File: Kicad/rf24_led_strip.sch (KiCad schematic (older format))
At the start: 27 parts, among them IC1 ATMEGA328-P, P1 UART, P2 12V in, P3 LED_OUT, Q1 Q_NMOS_GDS, Q2 Q_NMOS_GDS, Q3 Q_NMOS_GDS, U1 LM_1117, U2 LM_1117, U3 nrf24l01+

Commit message: 3.3V Version.
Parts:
- removed C2: C, Capacitors_SMD:C_0603_HandSoldering, symbol C
- removed R10, R11: R, Resistors_SMD:R_0805, symbol R
- removed U1: LM_1117, TO_SOT_Packages_SMD:SOT-223, symbol LM_1117
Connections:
- net labels removed: +5V
- wire segments 79 -> 71
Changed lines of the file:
@@
 	3550 4550 3300 4550
 Connection ~ 3550 4550
-$Comp
-L +5V #PWR05
-U 1 1 56C79115
-P 3300 2300
-F 0 "#PWR05" H 3300 2150 50  0001 C CNN
-F 1 "+5V" H 3300 2440 50  0000 C CNN
-F 2 "" H 3300 2300 60  0000 C CNN
-F 3 "" H 3300 2300 60  0000 C CNN
-	1    3300 2300
-	0    -1   -1   0
-$EndComp
 Wire Wire Line
 	3300 2300 3550 2300
@@
 Connection ~ 3350 2300
 $Comp
-L GND #PWR06
+L GND #PWR05
 U 1 1 56C7929B
 P 3350 2750
-F 0 "#PWR06" H 3350 2500 50  0001 C CNN
+F 0 "#PWR05" H 3350 2500 50  0001 C CNN
 F 1 "GND" H 3350 2600 50  0000 C CNN
 F 2 "" H 3350 2750 60  0000 C CNN
@@
 $EndComp
 $Comp
-L +12V #PWR07
+L +12V #PWR06
 U 1 1 56C796A5
-P 4600 1100
-F 0 "#PWR07" H 4600 950 50  0001 C CNN
-F 1 "+12V" H 4600 1240 50  0000 C CNN
-F 2 "" H 4600 1100 60  0000 C CNN
-F 3 "" H 4600 1100 60  0000 C CNN
-	1    4600 1100
-	0    -1   -1   0
-$EndComp
-$Comp
-L GND #PWR08
-U 1 1 56C796DA
 P 4700 1200
-F 0 "#PWR08" H 4700 950 50  0001 C CNN
-F 1 "GND" H 4700 1050 50  0000 C CNN
+F 0 "#PWR06" H 4700 1050 50  0001 C CNN
+F 1 "+12V" H 4700 1340 50  0000 C CNN
 F 2 "" H 4700 1200 60  0000 C CNN
 F 3 "" H 4700 1200 60  0000 C CNN
 	1    4700 1200
+	0    -1   -1   0
+$EndComp
+$Comp
+L GND #PWR07
+U 1 1 56C796DA
+P 4500 1100
+F 0 "#PWR07" H 4500 850 50  0001 C CNN
+F 1 "GND" H 4500 950 50  0000 C CNN
+F 2 "" H 4500 1100 60  0000 C CNN
+F 3 "" H 4500 1100 60  0000 C CNN
+	1    4500 1100
 	0    1    1    0
 $EndComp
@@
 	4700 1200 4850 1200
 Wire Wire Line
-	4600 1100 4850 1100
+	4500 1100 4850 1100
 $Comp
 L CONN_01X04 P3
@@
 $EndComp
 $Comp
-L +12V #PWR09
+L +12V #PWR08
 U 1 1 56C7A172
 P 5850 1100
-F 0 "#PWR09" H 5850 950 50  0001 C CNN
+F 0 "#PWR08" H 5850 950 50  0001 C CNN
 F 1 "+12V" H 5850 1240 50  0000 C CNN
 F 2 "" H 5850 1100 60  0000 C CNN
@@
 $EndComp
 $Comp
-L GND #PWR010
+L GND #PWR09
 U 1 1 56C7A8FA
 P 8150 4650
-F 0 "#PWR010" H 8150 4400 50  0001 C CNN
+F 0 "#PWR09" H 8150 4400 50  0001 C CNN
 F 1 "GND" H 8150 4500 50  0000 C CNN
 F 2 "" H 8150 4650 60  0000 C CNN
@@
 $EndComp
 $Comp
-L GND #PWR011
+L GND #PWR010
 U 1 1 56C7BD3D
 P 10250 4800
-F 0 "#PWR011" H 10250 4550 50  0001 C CNN
+F 0 "#PWR010" H 10250 4550 50  0001 C CNN
 F 1 "GND" H 10250 4650 50  0000 C CNN
 F 2 "" H 10250 4800 60  0000 C CNN
@@
 $EndComp
 $Comp
-L GND #PWR012
+L GND #PWR011
 U 1 1 56C7BF2D
 P 8150 5950
-F 0 "#PWR012" H 8150 5700 50  0001 C CNN
+F 0 "#PWR011" H 8150 5700 50  0001 C CNN
 F 1 "GND" H 8150 5800 50  0000 C CNN
 F 2 "" H 8150 5950 60  0000 C CNN
@@
 Wire Wire Line
 	6750 5450 7250 5450
-Text Label 6000 2300 2    60   ~ 0
+Text Label 6000 2500 2    60   ~ 0
 RED_PWM
 Wire Wire Line
@@
 Wire Wire Line
 	6000 2500 5450 2500
-Text Label 6000 2500 2    60   ~ 0
+Text Label 6000 2300 2    60   ~ 0
 BLUE_PWM
-Wire Wire Line
-	6000 2300 5450 2300
-$Comp
-L +5V #PWR013
-U 1 1 56C7D2C5
-P 6600 3750
-F 0 "#PWR013" H 6600 3600 50  0001 C CNN
-F 1 "+5V" H 6600 3890 50  0000 C CNN
-F 2 "" H 6600 3750 60  0000 C CNN
-F 3 "" H 6600 3750 60  0000 C CNN
-	1    6600 3750
-	0    1    1    0
-$EndComp
 $Comp
 L R R1
@@
 $EndComp
 $Comp
-L GND #PWR014
+L GND #PWR012
 U 1 1 56C7DDEB
 P 1900 3000
-F 0 "#PWR014" H 1900 2750 50  0001 C CNN
+F 0 "#PWR012" H 1900 2750 50  0001 C CNN
 F 1 "GND" H 1900 2850 50  0000 C CNN
 F 2 "" H 1900 3000 60  0000 C CNN
@@
 Wire Wire Line
 	2200 3000 2200 3300
+Text Label 2100 3000 3    60   ~ 0
+TX
 Text Label 2000 3000 3    60   ~ 0
-TX
-Text Label 2100 3000 3    60   ~ 0
 RX
 Wire Wire Line
@@
 	6100 4300 6100 4100
 $Comp
-L +12V #PWR015
+L +12V #PWR013
 U 1 1 56C7FD64
 P 1450 6300
-F 0 "#PWR015" H 1450 6150 50  0001 C CNN
+F 0 "#PWR013" H 1450 6150 50  0001 C CNN
 F 1 "+12V" H 1450 6440 50  0000 C CNN
 F 2 "" H 1450 6300 60  0000 C CNN
@@
 $EndComp
 $Comp
-L GND #PWR016
+L GND #PWR014
 U 1 1 56C7FDAE
 P 1750 6300
-F 0 "#PWR016" H 1750 6050 50  0001 C CNN
+F 0 "#PWR014" H 1750 6050 50  0001 C CNN
 F 1 "GND" H 1750 6150 50  0000 C CNN
 F 2 "" H 1750 6300 60  0000 C CNN
@@
 $EndComp
 $Comp
-L PWR_FLAG #FLG017
+L PWR_FLAG #FLG015
 U 1 1 56C7FEB7
 P 1450 6700
-F 0 "#FLG017" H 1450 6795 50  0001 C CNN
+F 0 "#FLG015" H 1450 6795 50  0001 C CNN
 F 1 "PWR_FLAG" H 1450 6880 50  0000 C CNN
 F 2 "" H 1450 6700 60  0000 C CNN
@@
 $EndComp
 $Comp
-L PWR_FLAG #FLG018
+L PWR_FLAG #FLG016
 U 1 1 56C7FF13
 P 1750 6700
-F 0 "#FLG018" H 1750 6795 50  0001 C CNN
+F 0 "#FLG016" H 1750 6795 50  0001 C CNN
 F 1 "PWR_FLAG" H 1750 6880 50  0000 C CNN
 F 2 "" H 1750 6700 60  0000 C CNN
@@
 NoConn ~ 3550 2900
 $Comp
-L +3.3V #PWR019
+L +3.3V #PWR017
 U 1 1 56C83337
 P 4650 5950
-F 0 "#PWR019" H 4650 5800 50  0001 C CNN
+F 0 "#PWR017" H 4650 5800 50  0001 C CNN
 F 1 "+3.3V" H 4650 6090 50  0000 C CNN
 F 2 "" H 4650 5950 60  0000 C CNN
@@
 MISO
 $Comp
-L GND #PWR020
+L GND #PWR018
 U 1 1 56C83AE6
 P 3300 5950
-F 0 "#PWR020" H 3300 5700 50  0001 C CNN
+F 0 "#PWR018" H 3300 5700 50  0001 C CNN
 F 1 "GND" H 3300 5800 50  0000 C CNN
 F 2 "" H 3300 5950 60  0000 C CNN
@@
 Wire Wire Line
 	8850 1200 8900 1200
-$Comp
-L R R10
-U 1 1 56D08DC0
-P 2000 1850
-F 0 "R10" V 2080 1850 50  0000 C CNN
-F 1 "R" V 2000 1850 50  0000 C CNN
-F 2 "Resistors_SMD:R_0805" V 1930 1850 30  0001 C CNN
-F 3 "" H 2000 1850 30  0000 C CNN
-	1    2000 1850
-	1    0    0    -1
-$EndComp
-$Comp
-L R R11
-U 1 1 56D08DC6
-P 2350 1700
-F 0 "R11" V 2430 1700 50  0000 C CNN
-F 1 "R" V 2350 1700 50  0000 C CNN
-F 2 "Resistors_SMD:R_0805" V 2280 1700 30  0001 C CNN
-F 3 "" H 2350 1700 30  0000 C CNN
-	1    2350 1700
-	0    -1   -1   0
-$EndComp
-Wire Wire Line
-	2000 1700 2000 1400
-$Comp
-L C C1
-U 1 1 56D08DCD
-P 1400 1400
-F 0 "C1" H 1425 1500 50  0000 L CNN
-F 1 "C" H 1425 1300 50  0000 L CNN
-F 2 "Capacitors_SMD:C_0603_HandSoldering" H 1438 1250 30  0001 C CNN
-F 3 "" H 1400 1400 60  0000 C CNN
-	1    1400 1400
-	-1   0    0    1
-$EndComp
-$Comp
-L C C2
-U 1 1 56D08DD3
-P 2500 1950
-F 0 "C2" H 2525 2050 50  0000 L CNN
-F 1 "C" H 2525 1850 50  0000 L CNN
-F 2 "Capacitors_SMD:C_0603_HandSoldering" H 2538 1800 30  0001 C CNN
-F 3 "" H 2500 1950 60  0000 C CNN
-	1    2500 1950
-	-1   0    0    1
-$EndComp
-Wire Wire Line
-	2500 900  2500 1800
-Wire Wire Line
-	1400 1550 1400 2100
-Connection ~ 2000 1700
-$Comp
-L +12V #PWR021
-U 1 1 56D08DDC
-P 1100 1000
-F 0 "#PWR021" H 1100 850 50  0001 C CNN
-F 1 "+12V" H 1100 1140 50  0000 C CNN
-F 2 "" H 1100 1000 60  0000 C CNN
-F 3 "" H 1100 1000 60  0000 C CNN
-	1    1100 1000
-	0    -1   -1   0
-$EndComp
-Wire Wire Line
-	2000 1700 2200 1700
-Wire Wire Line
-	1400 2100 2500 2100
-Wire Wire Line
-	2000 2000 2000 2250
-$Comp
-L GND #PWR022
-U 1 1 56D08DE5
-P 2000 2250
-F 0 "#PWR022" H 2000 2000 50  0001 C CNN
-F 1 "GND" H 2000 2100 50  0000 C CNN
-F 2 "" H 2000 2250 60  0000 C CNN
-F 3 "" H 2000 2250 60  0000 C CNN
-	1    2000 2250
-	1    0    0    -1
-$EndComp
-Connection ~ 2000 2100
-Connection ~ 2500 1700
-$Comp
-L LM_1117 U1
-U 1 1 56D08DF3
-P 1950 700
-F 0 "U1" H 2150 150 60  0000 C CNN
-F 1 "LM_1117" H 1950 700 60  0000 C CNN
-F 2 "TO_SOT_Packages_SMD:SOT-223" H 1950 700 60  0001 C CNN
-F 3 "" H 1950 700 60  0000 C CNN
-	1    1950 700
-	1    0    0    -1
-$EndComp
-Wire Wire Line
-	1100 1000 1550 1000
-Wire Wire Line
-	1400 1250 1400 1000
-Connection ~ 1400 1000
-Wire Wire Line
-	2450 1000 2800 1000
-Connection ~ 2500 1000
-Wire Wire Line
-	2450 900  2500 900
-$Comp
-L +5V #PWR023
-U 1 1 56D097BC
-P 2800 1000
-F 0 "#PWR023" H 2800 850 50  0001 C CNN
-F 1 "+5V" H 2800 1140 50  0000 C CNN
-F 2 "" H 2800 1000 60  0000 C CNN
-F 3 "" H 2800 1000 60  0000 C CNN
-	1    2800 1000
-	0    1    1    0
-$EndComp
 NoConn ~ 3550 3650
 NoConn ~ 3550 3750
@@
 NoConn ~ 5450 2900
 NoConn ~ 5450 3000
+$Comp
+L +3.3V #PWR019
+U 1 1 589CA4C6
+P 3300 2300
+F 0 "#PWR019" H 3300 2150 50  0001 C CNN
+F 1 "+3.3V" H 3300 2440 50  0000 C CNN
+F 2 "" H 3300 2300 60  0000 C CNN
+F 3 "" H 3300 2300 60  0000 C CNN
+	1    3300 2300
+	0    -1   -1   0
+$EndComp
+$Comp
+L +3.3V #PWR020
+U 1 1 589CAA46
+P 6600 3750
+F 0 "#PWR020" H 6600 3600 50  0001 C CNN
+F 1 "+3.3V" H 6600 3890 50  0000 C CNN
+F 2 "" H 6600 3750 60  0000 C CNN
+F 3 "" H 6600 3750 60  0000 C CNN
+	1    6600 3750
+	0    1    1    0
+$EndComp
+Wire Wire Line
+	5450 2300 6000 2300
+$Comp
+L C C1
+U 1 1 589CC8B0
+P 4500 5750
+F 0 "C1" H 4525 5850 50  0000 L CNN
+F 1 "C" H 4525 5650 50  0000 L CNN
+F 2 "Capacitors_SMD:C_0603_HandSoldering" H 4538 5600 30  0001 C CNN
+F 3 "" H 4500 5750 60  0000 C CNN
+	1    4500 5750
+	-1   0    0    1
+$EndComp
+$Comp
+L GND #PWR021
+U 1 1 589CCE09
+P 4500 5550
+F 0 "#PWR021" H 4500 5300 50  0001 C CNN
+F 1 "GND" H 4500 5400 50  0000 C CNN
+F 2 "" H 4500 5550 60  0000 C CNN
+F 3 "" H 4500 5550 60  0000 C CNN
+	1    4500 5550
+	-1   0    0    1
+$EndComp
+Wire Wire Line
+	4500 5600 4500 5550
+Wire Wire Line
+	4500 5900 4500 5950
+Connection ~ 4500 5950
 $EndSCHEMATC

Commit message: Update
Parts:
- added C10: 10µF, Capacitors_SMD:C_0805, symbol C
- added C11: 100µF, Capacitors_ThroughHole:CP_Radial_D6.3mm_P2.50mm, symbol CP
- added C2, C5: C, Capacitors_ThroughHole:C_Disc_D3.0mm_W2.0mm_P2.50mm, symbol C
- added C6, C9: C, Capacitors_SMD:C_0603_HandSoldering, symbol C
- added JP1: 5V, Connect:GS2, symbol Jumper_NO_Small
- added JP2: 12V, Connect:GS2, symbol Jumper_NO_Small
- added P4: LED3_OUT, Pin_Headers:Pin_Header_Straight_1x04_Pitch2.54mm, symbol CONN_01X04
- added P5: LED2_OUT, Pin_Headers:Pin_Header_Straight_1x04_Pitch2.54mm, symbol CONN_01X04
- added P6: WS2812, Pin_Headers:Pin_Header_Straight_1x03_Pitch2.54mm, symbol CONN_01X03
- added Q4, Q5, Q6, Q7, Q8, Q9: Q_NMOS_GDS, TO_SOT_Packages_SMD:SOT-23, symbol Q_NMOS_GSD
- added R10, R11, R12, R13, R14, R15, R16, R17, R18, R19, R20, R21, R22, R23, R24, R25, R26, R27: R, Resistors_SMD:R_0805, symbol R
- added U1: LM_1117, TO_SOT_Packages_SMD:SOT-223, symbol LM_1117
- added U4: ESP-01, Pin_Headers:Pin_Header_Straight_2x04_Pitch2.54mm, symbol ESP-01
- added Y1: Crystal, Crystals:Crystal_HC49-4H_Vertical, symbol Crystal
- C1: value C -> 100nF
- P1, P3: footprint Pin_Headers:Pin_Header_Straight_1x04 -> Pin_Headers:Pin_Header_Straight_1x04_Pitch2.54mm
- U3: footprint Socket_Strips:Socket_Strip_Straight_2x04 -> Pin_Headers:Pin_Header_Straight_2x04_Pitch2.54mm
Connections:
- net labels added: +5V, BLUE2, BLUE2_PWM, BLUE3, BLUE3_PWM, GREEN2, GREEN2_PWM, GREEN3, GREEN3_PWM, RED2, RED2_PWM, RED3, RED3_PWM, VCC
- wire segments 71 -> 164
- no-connect marks 14 -> 5
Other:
- moved on the sheet: C1, C3, C4, C7, C8, P1, P2, P3, Q1, Q2, Q3, R1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

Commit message: STM32 schematic done.
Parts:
- removed C11: 100µF, Capacitors_ThroughHole:CP_Radial_D6.3mm_P2.50mm, symbol CP
- removed C3, C4: C, Capacitors_SMD:C_0603_HandSoldering, symbol C
- removed IC1: ATMEGA328-P, Housings_QFP:TQFP-32_7x7mm_Pitch0.8mm, symbol ATMEGA328P-A
- removed JP1: 5V, Connect:GS2, symbol Jumper_NO_Small
- removed JP2: 12V, Connect:GS2, symbol Jumper_NO_Small
- removed P6: WS2812, Pin_Headers:Pin_Header_Straight_1x03_Pitch2.54mm, symbol CONN_01X03
- removed R1, R22: R, Resistors_SMD:R_0805, symbol R
- removed U1: LM_1117, TO_SOT_Packages_SMD:SOT-223, symbol LM_1117
- added C10: 10µF, Capacitors_SMD:C_0805, symbol C
- added C11, C12, C13, C14: 100nF, Capacitors_SMD:C_0603_HandSoldering, symbol C
- added D1: D, Diodes_ThroughHole:D_DO-15_P12.70mm_Horizontal, symbol D
- added JP1, JP2: Jumper, Pin_Headers:Pin_Header_Straight_1x02_Pitch2.54mm, symbol Jumper
- added P11: CONN_01X07, Pin_Headers:Pin_Header_Straight_1x07_Pitch2.54mm, symbol CONN_01X07
- added P5: LED4_OUT, Pin_Headers:Pin_Header_Straight_1x04_Pitch2.54mm, symbol CONN_01X04
- added P6: LED5_OUT, Pin_Headers:Pin_Header_Straight_1x04_Pitch2.54mm, symbol CONN_01X04
- added P7: USB_OTG, Connect:USB_Micro-B, symbol USB_OTG
- added P8: CONN_01X04, Pin_Headers:Pin_Header_Straight_1x04_Pitch2.54mm, symbol CONN_01X04
- added Q11, Q12, Q13, Q14, Q15, Q16: Q_NMOS_GDS, TO_SOT_Packages_SMD:SOT-23, symbol Q_NMOS_GSD
- added R26, R27, R28, R29, R30, R31, R32, R33, R34, R35, R36, R37, R40, R41: R, Resistors_SMD:R_0805, symbol R
- added U3: STM32F103C8Tx, Housings_QFP:LQFP-48_7x7mm_Pitch0.5mm, symbol STM32F103C8Tx
- C6, C9: value C -> 100nF
- renumbered C10 to C2, C5 to C4, C2 to C5, P2 to P1, P3 to P2, P5 to P3, P1 to P9, Q9 to Q10, Q1 to Q2, Q2 to Q4, Q4 to Q6, Q6 to Q7, Q7 to Q9, R12 to R11, R14 to R12, R15 to R14, R26 to R15, R27 to R16, R16 to R18, R18 to R19, R19 to R21, R21 to R22, R2 to R3, R6 to R38, R7 to R39, R8 to R4, R3 to R5, R4 to R6, R9 to R7, R5 to R8, R11 to R9, U3 to U1, U4 to U2, U2 to U4
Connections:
- net labels added: BLUE4, BLUE4_PWM, BLUE5, BLUE5_PWM, BOOT0, BOOT1, EXTRA1, EXTRA2, EXTRA3, EXTRA4, EXTRA5, EXTRA6, EXTRA7, GREEN4, GREEN4_PWM, GREEN5, GREEN5_PWM, NRST, RED4, RED4_PWM, RED5, RED5_PWM, SWD_CLK, SWD_IO, USB_DM, USB_DP
- net labels removed: +5V, DTR
- wire segments 164 -> 250
- no-connect marks 5 -> 4
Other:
- moved on the sheet: C1, C2, C4, C5, C7, C8, P1, P2, P3, P4, P9, Q10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

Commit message: First pcb version.
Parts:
- P8: value CONN_01X04 -> SWD; footprint Pin_Headers:Pin_Header_Straight_1x04_Pitch2.54mm -> Pin_Headers:Pin_Header_Straight_1x05_Pitch2.54mm; symbol CONN_01X04 -> CONN_01X05
- P9: footprint Pin_Headers:Pin_Header_Straight_1x04_Pitch2.54mm -> Pin_Headers:Pin_Header_Straight_1x03_Pitch2.54mm; symbol CONN_01X04 -> CONN_01X03
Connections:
- net +12V: now also P1.1 (P1); no longer P1.2 (P2)
- net +3V3: now also P8.5 (P5)
- net BLUE4_PWM: now also U3.46 (PB9/CAN_TX/I2C1_SDA/TIM4_CH4); no longer U3.42 (PB6/I2C1_SCL/TIM4_CH1/USART1_TX)
- net BLUE5_PWM: now also U3.42 (PB6/I2C1_SCL/TIM4_CH1/USART1_TX); no longer U3.46 (PB9/CAN_TX/I2C1_SDA/TIM4_CH4)
- net GND: now also P1.2 (P2), P8.2 (P2), P9.3 (P3); no longer P1.1 (P1), P8.1 (P1), P9.4 (P4)
- net GREEN4: now also Q13.3 (D); no longer Q16.3 (D)
- net GREEN4_PWM: now also U3.45 (PB8/CAN_RX/I2C1_SCL/TIM4_CH3); no longer U3.41 (PB5/I2C1_SMBA/SPI1_MOSI/TIM3_CH2)
- net GREEN5: now also Q16.3 (D); no longer Q13.3 (D)
- net GREEN5_PWM: now also U3.41 (PB5/I2C1_SMBA/SPI1_MOSI/TIM3_CH2); no longer U3.45 (PB8/CAN_RX/I2C1_SCL/TIM4_CH3)
- net NRST: now also P8.1 (P1); no longer P8.4 (P4)
- net RED4_PWM: now also U3.43 (PB7/I2C1_SDA/TIM4_CH2/USART1_RX); no longer U3.40 (PB4/SPI1_MISO/SYS_NJTRST/TIM3_CH1)
- net RED5_PWM: now also U3.40 (PB4/SPI1_MISO/SYS_NJTRST/TIM3_CH1); no longer U3.43 (PB7/I2C1_SDA/TIM4_CH2/USART1_RX)
- net RX: now also P9.2 (P2); no longer P9.3 (P3)
- net SWD_CLK: now also P8.3 (P3); no longer P8.2 (P2)
- net SWD_IO: now also P8.4 (P4); no longer P8.3 (P3)
- net TX: now also P9.1 (P1); no longer P9.2 (P2)
- no-connect marks 4 -> 3
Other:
- note added: "Wireless"
- moved on the sheet: C1, C2, P1, P2, P3, P4, P5, P6, Q10, Q11, Q12, Q13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

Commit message: First "complete" stm32 version.
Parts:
- added P10: CONN_01X04, Pin_Headers:Pin_Header_Straight_1x04_Pitch2.54mm, symbol CONN_01X04
- C4, C5: value C -> 22pF
- C7, C8: value C -> 100nF
- D1: footprint Diodes_ThroughHole:D_DO-15_P12.70mm_Horizontal -> Diodes_SMD:D_SOD-123
- P11: footprint Pin_Headers:Pin_Header_Straight_1x07_Pitch2.54mm -> Pin_Headers:Pin_Header_Straight_1x03_Pitch2.54mm; symbol CONN_01X07 -> CONN_01X03
- R10, R11, R17, R18, R19, R23, R24, R25, R29, R3, R30, R31, R4, R5, R9: value R -> 1k
- R12, R13, R14, R15, R16, R20, R21, R22, R26, R27, R28, R32, R33, R34, R40, R41, R6, R7, R8: value R -> 10k
- R35, R36: value R -> 22Ω
- R37: value R -> 1.5k
- U4: value LM_1117 -> AMS1117; symbol LM_1117 -> AMS1117
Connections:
- net +12V: now also U4.3 (Vin); no longer U4.1 (Vin)
- net +3V3: now also U4.2 (Vout); no longer U4.3 (Vout)
- net CE: now also U3.11 (ADC1_IN1/ADC2_IN1/TIM2_CH2/USART2_RTS/PA1); no longer U3.3 (PC14/RCC_OSC32_IN)
- net CSN: now also U3.10 (ADC1_IN0/ADC2_IN0/SYS_WKUP/TIM2_CH1/TIM2_ETR/USART2_CTS/PA0); no longer U3.2 (PC13/RTC_OUT/RTC_TAMPER)
- net EXTRA1: now also P10.4 (P4); no longer P11.1 (P1)
- net EXTRA2: now also P10.3 (P3); no longer P11.2 (P2)
- net EXTRA3: now also P10.2 (P2); no longer P11.3 (P3)
- net EXTRA4: now also P10.1 (P1); no longer P11.4 (P4)
- net EXTRA5: now also P11.3 (P3), U3.4 (PC15/ADC1_EXTI15/ADC2_EXTI15/RCC_OSC32_OUT); no longer P11.5 (P5), U3.10 (ADC1_IN0/ADC2_IN0/SYS_WKUP/TIM2_CH1/TIM2_ETR/USART2_CTS/PA0)
- net EXTRA6: now also P11.2 (P2), U3.3 (PC14/RCC_OSC32_IN); no longer P11.6 (P6), U3.11 (ADC1_IN1/ADC2_IN1/TIM2_CH2/USART2_RTS/PA1)
- net EXTRA7: now also P11.1 (P1), U3.2 (PC13/RTC_OUT/RTC_TAMPER); no longer P11.7 (P7), U3.14 (ADC1_IN4/ADC2_IN4/SPI1_NSS/USART2_CK/PA4)
- net IRQ: now also U3.14 (ADC1_IN4/ADC2_IN4/SPI1_NSS/USART2_CK/PA4); no longer U3.4 (PC15/ADC1_EXTI15/ADC2_EXTI15/RCC_OSC32_OUT)
- net at R38.1, R39.1: now also U4.1 (ADJ); no longer U4.2 (ADJ)
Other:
- note added: "Boot config"
- note added: "Debug"
- note added: "Extra connectors"
- note added: "LED connectors"
- note added: "Power"
- note added: "Transistors"
- note added: "USB"
- note added: "µC Filtering"
- moved on the sheet: C10, C11, C12, C13, C14, C4, C5, C6, C7, C8, C9, D1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

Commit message: Fix micro usb.
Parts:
- P7: footprint Connect:USB_Micro-B -> Connectors_Molex:USB_Micro-B_Molex_47346-0001
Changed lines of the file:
@@
 F 0 "P7" H 3825 7075 50  0000 C CNN
 F 1 "USB_OTG" H 3500 7400 50  0000 C CNN
-F 2 "Connect:USB_Micro-B" V 3450 7100 50  0001 C CNN
+F 2 "Connectors_Molex:USB_Micro-B_Molex_47346-0001" V 3450 7100 50  0001 C CNN
 F 3 "" V 3450 7100 50  0000 C CNN
 	1    3500 7200

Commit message: Update power supply.
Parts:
- added C3: 10µF, Capacitors_SMD:C_0805, symbol C
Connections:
- net +3V3: now also C3.2
- net GND: now also C3.1
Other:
- note added: "Note: Please use external fuse. No space for it"

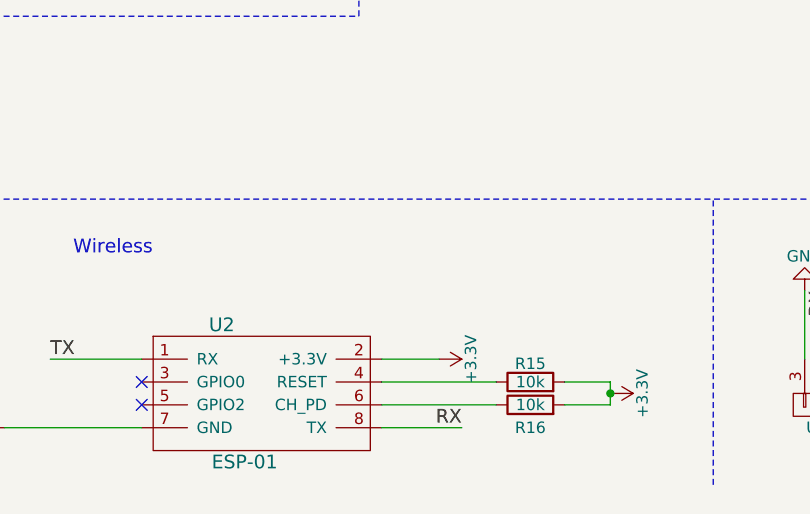
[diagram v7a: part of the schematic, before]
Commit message: Add capacitors to the ESP8266.
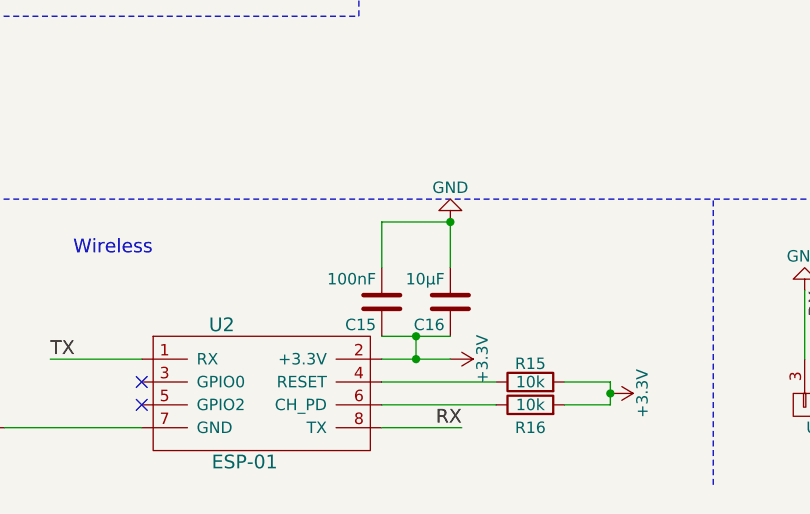
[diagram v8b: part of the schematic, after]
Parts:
- added C15: 100nF, Capacitors_SMD:C_0603_HandSoldering, symbol C
- added C16: 10µF, Capacitors_SMD:C_0805, symbol C
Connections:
- net +3V3: now also C15.1, C16.1
- net GND: now also C15.2, C16.2
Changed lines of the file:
@@
 L +3.3V #PWR022
 U 1 1 589DA6B3
-P 5000 10650
-F 0 "#PWR022" H 5000 10500 50  0001 C CNN
-F 1 "+3.3V" H 5000 10790 50  0000 C CNN
-F 2 "" H 5000 10650 60  0000 C CNN
-F 3 "" H 5000 10650 60  0000 C CNN
-	1    5000 10650
+P 5050 10650
+F 0 "#PWR022" H 5050 10500 50  0001 C CNN
+F 1 "+3.3V" H 5050 10790 50  0000 C CNN
+F 2 "" H 5050 10650 60  0000 C CNN
+F 3 "" H 5050 10650 60  0000 C CNN
+	1    5050 10650
 	0    1    1    0
 $EndComp
@@
 	-1   0    0    1
 $EndComp
+Text Notes 2400 4900 0    60   ~ 0
+Note: Please use external fuse. No space for it
+$Comp
+L C C3
+U 1 1 58D56B58
+P 2750 6150
+F 0 "C3" H 2775 6250 50  0000 L CNN
+F 1 "10µF" H 2775 6050 50  0000 L CNN
+F 2 "Capacitors_SMD:C_0805" H 2788 6000 30  0001 C CNN
+F 3 "" H 2750 6150 60  0000 C CNN
+	1    2750 6150
+	-1   0    0    1
+$EndComp
 Wire Wire Line
 	14100 8450 15150 8450
@@
 	3100 10950 3700 10950
 Wire Wire Line
-	4750 10650 5000 10650
+	4750 10650 5050 10650
 Wire Wire Line
 	6950 6650 6950 6350
@@
 Wire Wire Line
 	3450 6100 3450 6250
-Text Notes 2400 4900 0    60   ~ 0
-Note: Please use external fuse. No space for it
-$Comp
-L C C3
-U 1 1 58D56B58
-P 2750 6150
-F 0 "C3" H 2775 6250 50  0000 L CNN
-F 1 "10µF" H 2775 6050 50  0000 L CNN
-F 2 "Capacitors_SMD:C_0805" H 2788 6000 30  0001 C CNN
-F 3 "" H 2750 6150 60  0000 C CNN
-	1    2750 6150
-	-1   0    0    1
-$EndComp
 Wire Wire Line
 	2750 6000 2750 5950
@@
 	2750 6350 2750 6300
 Connection ~ 2450 6350
+$Comp
+L C C15
+U 1 1 58D5C298
+P 4750 10400
+F 0 "C15" H 4775 10500 50  0000 L CNN
+F 1 "100nF" H 4775 10300 50  0000 L CNN
+F 2 "Capacitors_SMD:C_0603_HandSoldering" H 4788 10250 30  0001 C CNN
+F 3 "" H 4750 10400 60  0000 C CNN
+	1    4750 10400
+	-1   0    0    1
+$EndComp
+$Comp
+L GND #PWR057
+U 1 1 58D5C29E
+P 5050 10050
+F 0 "#PWR057" H 5050 9800 50  0001 C CNN
+F 1 "GND" H 5050 9900 50  0000 C CNN
+F 2 "" H 5050 10050 60  0000 C CNN
+F 3 "" H 5050 10050 60  0000 C CNN
+	1    5050 10050
+	-1   0    0    1
+$EndComp
+$Comp
+L C C16
+U 1 1 58D5C2A4
+P 5050 10400
+F 0 "C16" H 5075 10500 50  0000 L CNN
+F 1 "10µF" H 5075 10300 50  0000 L CNN
+F 2 "Capacitors_SMD:C_0805" H 5088 10250 30  0001 C CNN
+F 3 "" H 5050 10400 60  0000 C CNN
+	1    5050 10400
+	-1   0    0    1
+$EndComp
+Connection ~ 5050 10050
+Wire Wire Line
+	5050 10050 5050 10250
+Wire Wire Line
+	4750 10050 4750 10250
+Wire Wire Line
+	4750 10050 5050 10050
+Wire Wire Line
+	4750 10550 5050 10550
+Wire Wire Line
+	4900 10550 4900 10650
+Connection ~ 4900 10650
+Connection ~ 4900 10550
 $EndSCHEMATC
